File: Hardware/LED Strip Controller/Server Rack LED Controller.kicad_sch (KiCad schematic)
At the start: 76 parts

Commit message: Adding hardware schematic changes, added power regulation circuitry, stm32 filtering caps, labels
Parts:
- removed J?: Jack-DC, symbol Connector:Jack-DC
- added C10, C12, C13, C22, C27, C6, C8: 100nF, symbol Device:C
- added C11, C16: 100nF, Capacitor_SMD:C_1206_3216Metric_Pad1.33x1.80mm_HandSolder, symbol Device:C
- added C15, C9: 10nF, Capacitor_SMD:C_1206_3216Metric_Pad1.33x1.80mm_HandSolder, symbol Device:C
- added C17: 220u, Capacitor_SMD:CP_Elec_6.3x7.7, symbol Device:C_Polarized
- added C18, C20: 10uF, symbol Device:C_Polarized
- added C2, C23, C24, C3: C, symbol Device:C
- added C21, C25: 1uF, symbol Device:C
- added C4: 100uF, symbol Device:C_Polarized
- added C5: 1000u, Capacitor_SMD:CP_Elec_10x10.5, symbol Device:C_Polarized
- added C7: 680u, Capacitor_SMD:CP_Elec_6.3x7.7, symbol Device:C_Polarized
- added D13: 1N5821, Diode_SMD:D_SMA, symbol Diode:1N5821
- added D15, D22: LED, symbol Device:LED
- added D21: STPS2L30A, symbol pspice:DIODE
- added F1: Fuse, symbol Device:Fuse
- added FB?: FerriteBead, symbol Device:FerriteBead
- added J10, J5: Conn_01x03_Female, symbol Connector:Conn_01x03_Female
- added J15: Conn_01x06_Female, symbol Connector:Conn_01x06_Female
- added J4: Conn_02x03_Odd_Even, symbol Connector_Generic:Conn_02x03_Odd_Even
- added J8: Conn_01x04_Male, symbol Connector:Conn_01x04_Male
- added J9: USB_B_Micro, symbol Connector:USB_B_Micro
- added L1: 22u, Inductor_SMD:L_12x12mm_H8mm, symbol Device:L
- added Q3: Q_PMOS_SDG, Package_TO_SOT_SMD:TO-252-3_TabPin2, symbol Device:Q_PMOS_GDS
- added R14, R16, R22: R, symbol Device:R
- added R29, R30, R31, R32: 10K, symbol Device:R
- added R7: 10K, Resistor_SMD:R_1206_3216Metric_Pad1.30x1.75mm_HandSolder, symbol Device:R
- added SW1: SW_Push_Dual, symbol Switch:SW_Push_Dual
- added U2: LM2596S-5, Package_TO_SOT_SMD:TO-263-5_TabPin3, symbol Regulator_Switching:LM2596S-5
- added U3: LD1117S50TR_SOT223, Package_TO_SOT_SMD:SOT-223-3_TabPin2, symbol Regulator_Linear:LD1117S50TR_SOT223
- added U4: LD39050PU33R, SON95P300X300X100-7N, symbol LD39050PU33R:LD39050PU33R
- added Y1: Crystal, symbol Device:Crystal
- gave numbers to parts that had none: 75
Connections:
- net +5V: now also C21.1, C22.1, D21.2 (A), R22.1, U4.1 (EN), U4.6 (VIN); no longer J1.1 (Pin_1), J12.1 (Pin_1), J14.1 (Pin_1), J7.1 (Pin_1)
- net GND: now also C10.2, C11.2, C12.2, C13.2, C15.2, C16.2, C17.2, C18.2, C2.2, C20.2, C21.2, C22.2, C23.2, C24.2, C25.2, C27.2, C3.2, C4.2, C5.2, C6.2, C7.2, C8.2, C9.2, D13.2 (A), D15.1 (K), D22.1 (K), J10.3 (Pin_3), J15.6 (Pin_6), J4.1 (Pin_1), J4.2 (Pin_2), J5.3 (Pin_3), J8.4 (Pin_4), J9.5 (GND), J9.6 (Shield), R7.2, SW1.3, SW1.4, U2.3 (GND), U2.5 (~{ON}/OFF), U3.1 (GND), U4.2 (GND), U4.7 (GND)
- net PWM_1_BLUE: now also U1.17 (PA7)
- net PWM_1_GREEN: now also U1.19 (PB1)
- net PWM_1_RED: now also U1.18 (PB0)
- net PWM_2_BLUE: now also U1.11 (PA1)
- net PWM_2_GREEN: now also U1.13 (PA3)
- net PWM_2_RED: now also U1.12 (PA2)
- net PWM_3_BLUE: now also U1.45 (PB8)
- net PWM_3_GREEN: now also U1.42 (PB6)
- net PWM_3_RED: now also U1.43 (PB7)
- net PWM_4_BLUE: now also U1.46 (PB9)
- net PWM_4_GREEN: now also U1.10 (PA0)
- net PWM_4_RED: now also U1.16 (PA6)
- net STATUS_LED: now reaches U1.2 (PC13)
- net BOOT1: now reaches U1.20 (PB2)
- net BOOT1: now also J4.3 (Pin_3)
- net STM32_SCL2: now reaches U1.21 (PB10)
- net STM32_SCL2: now also J5.1 (Pin_1)
- net STM32_SDA2: now reaches U1.22 (PB11)
- net STM32_SDA2: now also J5.2 (Pin_2)
- net BUTTON_1: now reaches U1.26 (PB13)
- net BUTTON_1: now also J15.2 (Pin_2), R29.2
- net BUTTON_2: now reaches U1.27 (PB14)
- net BUTTON_2: now also J15.3 (Pin_3), R30.2
- net BUTTON_3: now reaches U1.28 (PB15)
- net BUTTON_3: now also J15.4 (Pin_4), R31.2
- net BUTTON_4: now reaches U1.29 (PA8)
- net BUTTON_4: now also J15.5 (Pin_5), R32.2
- net at U1.3 (PC14): now also C2.1, Y1.1
- net STM32_TX1: now reaches U1.30 (PA9)
- net STM32_TX1: now also J10.1 (Pin_1)
- net STM32_RX1: now reaches U1.31 (PA10)
- net STM32_RX1: now also J10.2 (Pin_2)
- net at U1.32 (PA11): now also J9.2 (D-)
- net at U1.33 (PA12): now also J9.3 (D+)
- net at U1.34 (PA13): now also J8.2 (Pin_2)
- net at U1.37 (PA14): now also J8.3 (Pin_3)
- net at U1.4 (PC15): now also C3.1, Y1.2
- net BOOT0: now reaches U1.44 (BOOT0)
- net BOOT0: now also J4.4 (Pin_4)
- net +VDC: no longer names the net of J3.1 (Pin_1)
- net +VDC: now also Q3.2 (D)
- new net: C20.1, D21.1 (K), U3.2 (VO)
- new net: D13.1 (K), L1.1, U2.2 (OUT)
- new net: F1.1, Q3.3 (S)
- new net: D22.2 (A), R22.2
- new net: FB?.1, U4.4 (VOUT)
- new net: Q3.1 (G), R7.1
- new net: D15.2 (A), R16.2
- new net: R14.2, SW1.1, SW1.2
- new net +3V3: C23.1, C24.1, C25.1, C27.1, FB?.2, J15.1 (Pin_1), R29.1, R30.1, R31.1, R32.1
- new net SMPS_5V: C15.1, C16.1, C17.1, J1.1 (Pin_1), J12.1 (Pin_1), J14.1 (Pin_1), J7.1 (Pin_1), L1.2, U2.4 (FB)
- new net VDD: C10.1, C12.1, C4.1, C6.1, C8.1, J4.5 (Pin_5), J4.6 (Pin_6), J8.1 (Pin_1), R14.1
- new net VDDA: C13.1
- new net Vss: C11.1, C18.1, C5.1, C7.1, C9.1, F1.2, U2.1 (VIN), U3.3 (VI)
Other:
- note added: "Input Power Circuitry"
- note added: "LED Strip Four"
- note added: "STM32 MCU Power"
- note removed: "Power Connectors"
- note removed: "SMPS"
- moved on the sheet: J14, J2, J3, J7, U1

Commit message: Adding updated PCB Schematic, still to add USB C connector and JLCPCB Part Numbers and values
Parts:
- removed J10: Conn_01x03_Female, symbol Connector:Conn_01x03_Female
- added C28, C31, C32: C, symbol Device:C
- added C29: 01.uF, Capacitor_SMD:C_1206_3216Metric, symbol Device:C
- added C30: 1uF, Capacitor_SMD:C_1206_3216Metric, symbol Device:C
- added D29: LED, symbol Device:LED
- added D30, D31: DIODE, symbol pspice:DIODE
- added J10: UART, Connector_PinHeader_2.54mm:PinHeader_1x03_P2.54mm_Vertical, symbol Connector:Conn_01x03_Male
- added J17: TST, symbol Connector:Conn_01x05_Male
- added J18, J19: Conn_01x03_Male, Connector_PinHeader_2.54mm:PinHeader_1x03_P2.54mm_Vertical, symbol Connector:Conn_01x03_Male
- added P1: USB_C_Plug, Connector_USB:USB_C_Receptacle_GCT_USB4085, symbol Connector:USB_C_Plug
- added Q14: IRF540N, Package_TO_SOT_THT:TO-220-3_Vertical, symbol Transistor_FET:IRF540N
- added R33, R34, R35, R36, R40, R41: R, symbol Device:R
- added R37, R39: 100K, Resistor_SMD:R_1206_3216Metric, symbol Device:R
- added R38: R, Resistor_SMD:R_1206_3216Metric, symbol Device:R
- added R42, R43, R46, R47: 20R, Resistor_SMD:R_1206_3216Metric, symbol Device:R
- added R44: 4.7K, Resistor_SMD:R_1206_3216Metric, symbol Device:R
- added R45: 1M, Resistor_SMD:R_1206_3216Metric, symbol Device:R
- added R48: 4.7K, symbol Device:R
- added U5: INA169, Package_TO_SOT_SMD:SOT-23-5, symbol Amplifier_Current:INA169
- added Y2: 8MHz, symbol Device:Crystal
- C1, C26: footprint (none) -> Capacitor_SMD:CP_Elec_10x10.5
- C10, C12, C13, C21, C22, C25, C27, C6, C8: footprint (none) -> Capacitor_SMD:C_1206_3216Metric
- C23: value C -> 100nF; footprint (none) -> Capacitor_SMD:C_1206_3216Metric
- C24: value C -> 10nF; footprint (none) -> Capacitor_SMD:C_1206_3216Metric
- D15, D22: footprint (none) -> LED_SMD:LED_1206_3216Metric
- J1, J12, J14, J7: footprint (none) -> Connector_PinHeader_2.54mm:PinHeader_1x03_P2.54mm_Vertical
- J11, J13, J16, J6: footprint (none) -> Connector_JST:JST_EH_B4B-EH-A_1x04_P2.50mm_Vertical
- J4: footprint (none) -> Connector_PinHeader_2.54mm:PinHeader_2x03_P2.54mm_Vertical
- J5: footprint (none) -> Connector_PinHeader_2.54mm:PinHeader_1x03_P2.54mm_Vertical; symbol Connector:Conn_01x03_Female -> Connector:Conn_01x03_Male
- J8: value Conn_01x04_Male -> SWD; footprint (none) -> Connector_PinHeader_2.54mm:PinHeader_1x04_P2.54mm_Vertical
- J9: footprint (none) -> Connector_USB:USB_Micro-B_Molex-105017-0001
- R1, R16, R2, R22, R23, R24, R25, R26, R27, R28, R29, R3, R30, R31, R32, R4, R5, R6: footprint (none) -> Resistor_SMD:R_1206_3216Metric
- R14: value R -> 10K; footprint (none) -> Resistor_SMD:R_1206_3216Metric
- SW1: footprint (none) -> Button_Switch_THT:SW_PUSH_6mm
- gave numbers to parts that had none: 1
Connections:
- net VDD is gone; now on net +3V3: C10.1, C12.1, C4.1, C6.1, C8.1, J4.5 (Pin_5), J4.6 (Pin_6), J8.1 (Pin_1), R14.1
- net VDDA is gone; now on net +3V3: C13.1
- net +3V3: now also R16.1, U1.24 (VDD), U1.36 (VDD), U1.48 (VDD), U1.9 (VDDA), C28.1, C29.1, J17.4 (Pin_4), U5.5 (V+)
- net +5V: now also J17.3 (Pin_3)
- net BOOT0: now also R39.2; no longer J4.4 (Pin_4)
- net BOOT1: now also R37.1; no longer J4.3 (Pin_3)
- net GND: now also U1.14 (PA4), U1.23 (VSS), U1.35 (VSS), U1.47 (VSS), U1.8 (VSSA), C28.2, C29.2, C30.2, C31.2, C32.2, D29.1 (K), J10.3 (Pin_3), J17.5 (Pin_5), P1.A1 (GND), P1.A12 (GND), P1.B1 (GND), P1.B12 (GND), Q14.3 (S), R34.1, R36.1, R41.2, U5.2 (GND)
- net PWM_1_BLUE: now also U1.12 (PA2); no longer U1.17 (PA7)
- net PWM_1_GREEN: now also U1.10 (PA0); no longer U1.19 (PB1)
- net PWM_1_RED: now also U1.11 (PA1); no longer U1.18 (PB0)
- net PWM_2_BLUE: now also U1.17 (PA7), U1.18 (PB0); no longer U1.11 (PA1)
- net PWM_2_GREEN: now also U1.16 (PA6); no longer U1.13 (PA3)
- net PWM_2_RED: no longer U1.12 (PA2)
- net PWM_4_GREEN: now also U1.13 (PA3); no longer U1.10 (PA0)
- net PWM_4_RED: now also U1.19 (PB1); no longer U1.16 (PA6)
- net SMPS_5V: now also D30.2 (A), J17.2 (Pin_2)
- net STATUS_LED: now also R38.1
- net STM32_RX1: now also J10.2 (Pin_2)
- net STM32_TX1: now also J10.1 (Pin_1)
- net Vss: now also J17.1 (Pin_1), R33.2, R35.2, U5.4 (-); no longer F1.2
- net OSC32_OUT: now reaches C3.1, U1.4 (PC15), Y1.2
- net OSC32_OUT: now also R45.2
- net USB_5V: now reaches J9.1 (VBUS)
- net USB_5V: now also R44.2, R48.2
- net at J9.2 (D-): now also R43.2; no longer U1.32 (PA11)
- net at J9.3 (D+): now also R42.2, R44.1; no longer U1.33 (PA12)
- net OSC32_IN: now reaches C2.1, U1.3 (PC14), Y1.1
- net OSC32_IN: now also R45.1
- net VS_SENSE: now reaches U1.15 (PA5)
- net VS_SENSE: now also R35.1, R36.2
- net FAN_SIG: now reaches U1.38 (PA15)
- net FAN_SIG: now also D31.2 (A), R40.2
- net OSC_IN: now reaches U1.5 (PD0)
- net OSC_IN: now also C31.1, Y2.1
- net OSC_OUT: now reaches U1.6 (PD1)
- net OSC_OUT: now also C32.1, Y2.2
- net RESET: now reaches U1.7 (NRST)
- net RESET: now also R14.2, SW1.1, SW1.2, C30.1
- new net: D29.2 (A), R38.2
- new net: D31.1 (K), Q14.1 (G), R40.1, R41.1
- new net: R34.2, U5.1
- new net: F1.2, R33.1, U5.3 (+)
- new net: R46.2, R48.1
- new net: D30.1 (K), Q14.2 (D)
- new net: J4.4 (Pin_4), R39.1
- new net: J4.3 (Pin_3), R37.2
- new net: P1.A4 (VBUS), P1.A9 (VBUS), P1.B4 (VBUS), P1.B9 (VBUS)
- new net STM32_USB+: J18.2 (Pin_2), U1.33 (PA12)
- new net STM32_USB-: J19.2 (Pin_2), U1.32 (PA11)
- new net STM32_USB_C+: J18.1 (Pin_1), J19.1 (Pin_1), R46.1
- new net STM32_USB_C-: R47.1
- new net STM32_USB_MICRO+: J18.3 (Pin_3), R42.1
- new net STM32_USB_MICRO-: J19.3 (Pin_3), R43.1
- no-connect marks 0 -> 4
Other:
- note added: "Boot"
- note added: "Button Daughterboard Connector"
- note added: "Fan Controller"
- note added: "RESET"
- note added: "USB C"
- note added: "USB Micro"
- note added: "USB Selector"
- moved on the sheet: C2, C3, D15, F1, J2, J3, J4, J8, J9, Q3, R14, R16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

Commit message: Adding updated PCB Schematic, need to source JLCPCB SMT Parts and do layout
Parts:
- removed J18, J19: Conn_01x03_Male, Connector_PinHeader_2.54mm:PinHeader_1x03_P2.54mm_Vertical, symbol Connector:Conn_01x03_Male
- removed P1: USB_C_Plug, Connector_USB:USB_C_Receptacle_GCT_USB4085, symbol Connector:USB_C_Plug
- removed R46, R47: 20R, Resistor_SMD:R_1206_3216Metric, symbol Device:R
- removed R48: 4.7K, symbol Device:R
- added C33: 1u, Capacitor_SMD:C_1206_3216Metric, symbol Device:C
- added C34: 10n, Capacitor_SMD:C_1206_3216Metric, symbol Device:C
- added J18: Conn_01x02_Female, Connector_JST:JST_EH_B2B-EH-A_1x02_P2.50mm_Vertical, symbol Connector:Conn_01x02_Female
- added L2: 39n, symbol pspice:INDUCTOR
- added U6: USBLC6-2SC6, Package_TO_SOT_SMD:SOT-23-6, symbol Power_Protection:USBLC6-2SC6
- C1, C26: value C_Polarized -> 100uF
- C14, C19: value C_Polarized -> 100uF; footprint (none) -> Capacitor_SMD:CP_Elec_10x10
- C18: footprint (none) -> Capacitor_SMD:CP_Elec_10x10.5
- C2, C3, C31, C32: footprint (none) -> Capacitor_SMD:C_1206_3216Metric
- C20, C4: footprint (none) -> Capacitor_SMD:CP_Elec_10x10
- C28: value C -> 01.uF; footprint (none) -> Capacitor_SMD:C_1206_3216Metric
- D1: value DIODE -> 1N4148; footprint (none) -> Diode_SMD:D_SOD-323; LCSC (none) -> C2128
- D10, D12, D17, D18, D20, D25, D26, D28, D9: value DIODE -> 1N4001; footprint (none) -> Diode_SMD:D_SMA
- D11, D14, D16, D19, D2, D23, D24, D27, D31, D5, D7, D8: value DIODE -> 1N4148; footprint (none) -> Diode_SMD:D_SOD-323
- D15: value LED -> Green LED
- D22: value LED -> Blue LED
- D29: value LED -> RED LED; footprint (none) -> LED_SMD:LED_1206_3216Metric
- D3, D4: value DIODE -> 1N4001; footprint (none) -> Diode_SMD:D_SOD-123F
- D30: value DIODE -> 1N5001; footprint (none) -> Diode_SMD:D_SMA
- D6: value DIODE -> 1N4001; footprint (none) -> Diode_SMD:D_SOD-123F; LCSC (none) -> C162732
- F1: value Fuse -> 1A; footprint (none) -> Fuse:Fuseholder_Clip-5x20mm_Eaton_1A5601-01_Inline_P20.80x6.76mm_D1.70mm_Horizontal
- J15: footprint (none) -> Connector_JST:JST_EH_B6B-EH-A_1x06_P2.50mm_Vertical
- J17: footprint (none) -> Connector_PinHeader_2.54mm:PinHeader_1x05_P2.54mm_Vertical
- J2, J3: footprint (none) -> TerminalBlock:TerminalBlock_bornier-2_P5.08mm
- Q1: value IRF540N -> IRF510N; footprint Package_TO_SOT_THT:TO-220-3_Vertical -> Package_TO_SOT_SMD:TO-263-3_TabPin2
- Q10, Q11, Q12, Q13, Q14, Q2, Q4, Q5, Q6, Q7, Q8, Q9: value IRF540N -> IRF510N; footprint Package_TO_SOT_THT:TO-220-3_Vertical -> Package_TO_SOT_SMD:TO-263-2
- R10, R11, R15, R18, R19, R34, R40, R8: value R -> 10K; footprint (none) -> Resistor_SMD:R_1206_3216Metric
- R12, R13, R17, R20, R21, R41, R9: value R -> 100K; footprint (none) -> Resistor_SMD:R_1206_3216Metric
- R16, R22, R38: value R -> 15K
- R23, R25, R26, R3, R4: value R -> 10K
- R24, R27, R28, R5, R6: value R -> 100K
- R33: value R -> 0.1R; footprint (none) -> Resistor_SMD:R_2512_6332Metric
- R35: value R -> 1M; footprint (none) -> Resistor_SMD:R_1206_3216Metric
- R36: value R -> 10M; footprint (none) -> Resistor_SMD:R_1206_3216Metric
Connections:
- net +3V3: now also L2.1; no longer C13.1, U1.9 (VDDA)
- net GND: now also C33.2, C34.2, U6.2 (GND); no longer J9.6 (Shield)
- net STM32_USB+: now also U6.1 (I/O1)
- net STM32_USB-: now also U6.6 (I/O1)
- net STM32_USB_MICRO+: now also U6.3 (I/O2)
- net STM32_USB_MICRO-: now also U6.4 (I/O2)
- net at D30.1 (K), Q14.2 (D): now also J18.2 (Pin_2)
- net SMPS_5V renamed PWR_5V
- net PWR_5V: now also J18.1 (Pin_1)
- net USB_5V renamed USB_VBUS
- net USB_VBUS: now also U6.5 (VBUS)
- new net VDDA: C13.1, C33.1, C34.1, L2.2, U1.9 (VDDA)
- no-connect marks 4 -> 8
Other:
- note added: "Analogue Power Filtering"
- note added: "D"
- note added: "G"
- note added: "MCU Power Filtering"
- note added: "MCU Power and GND"
- note added: "S"
- note added: "STM32 Power LED"
- note removed: "USB C"
- note removed: "USB Selector"
- moved on the sheet: C10, C11, C12, C13, C15, C16, C17, C28, C29, C4, C5, C6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

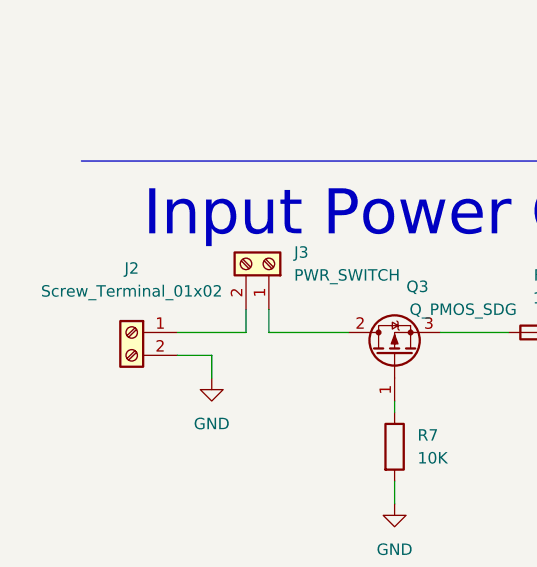
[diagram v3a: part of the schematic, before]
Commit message: Adding Kicad Schematic progress
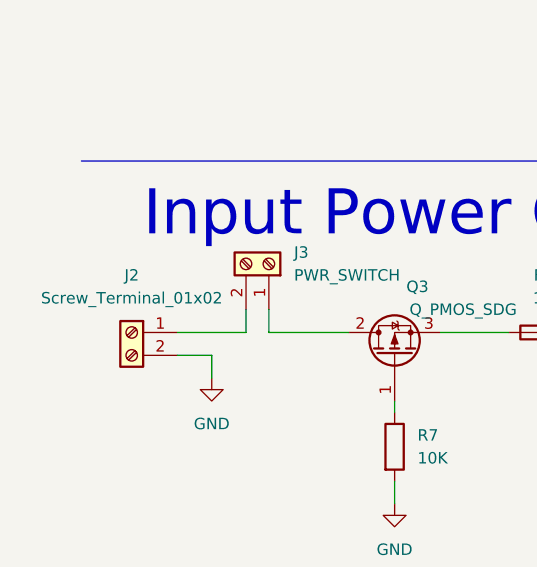
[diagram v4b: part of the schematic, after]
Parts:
- J2, J3: footprint TerminalBlock:TerminalBlock_bornier-2_P5.08mm -> TerminalBlock_Phoenix:TerminalBlock_Phoenix_MKDS-1,5-2-5.08_1x02_P5.08mm_Horizontal
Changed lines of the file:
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@@
   (symbol (lib_id "Connector:Screw_Terminal_01x02") (at 17.78 509.27 0) (mirror y) (unit 1)
     (in_bom yes) (on_board yes) (fields_autoplaced)
-    (property "Reference" "J2" (id 0) (at 17.78 502.158 0))
-    (property "Value" "Screw_Terminal_01x02" (id 1) (at 17.78 504.698 0))
-    (property "Footprint" "TerminalBlock:TerminalBlock_bornier-2_P5.08mm" (id 2) (at 17.78 509.27 0)
+    (property "Reference" "J2" (id 0) (at 17.78 502.92 0))
+    (property "Value" "Screw_Terminal_01x02" (id 1) (at 17.78 505.46 0))
+    (property "Footprint" "TerminalBlock_Phoenix:TerminalBlock_Phoenix_MKDS-1,5-2-5.08_1x02_P5.08mm_Horizontal" (id 2) (at 17.78 509.27 0)
       (effects (font (size 1.27 1.27)) hide)
     )
@@
       (effects (font (size 1.27 1.27)) (justify left))
     )
-    (property "Footprint" "TerminalBlock:TerminalBlock_bornier-2_P5.08mm" (id 2) (at 33.02 501.65 0)
+    (property "Footprint" "TerminalBlock_Phoenix:TerminalBlock_Phoenix_MKDS-1,5-2-5.08_1x02_P5.08mm_Horizontal" (id 2) (at 33.02 501.65 0)
       (effects (font (size 1.27 1.27)) hide)
     )
@@
     )
     (path "/b3c3b2d3-c28f-482e-9e67-413fada49294"
-      (reference "J2") (unit 1) (value "Screw_Terminal_01x02") (footprint "TerminalBlock:TerminalBlock_bornier-2_P5.08mm")
+      (reference "J2") (unit 1) (value "Screw_Terminal_01x02") (footprint "TerminalBlock_Phoenix:TerminalBlock_Phoenix_MKDS-1,5-2-5.08_1x02_P5.08mm_Horizontal")
     )
     (path "/b6d23dff-3660-46df-872f-37068fda7fff"
-      (reference "J3") (unit 1) (value "PWR_SWITCH") (footprint "TerminalBlock:TerminalBlock_bornier-2_P5.08mm")
+      (reference "J3") (unit 1) (value "PWR_SWITCH") (footprint "TerminalBlock_Phoenix:TerminalBlock_Phoenix_MKDS-1,5-2-5.08_1x02_P5.08mm_Horizontal")
     )
     (path "/7c1a5b26-d178-45d7-93d6-d3f5f5b864d0"

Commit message: Started layout of PCB
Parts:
- added C100, C39: 100uF, Capacitor_SMD:CP_Elec_6.3x7.7, symbol Device:C_Polarized
- added C35, C37: 10nF, Capacitor_SMD:C_1206_3216Metric_Pad1.33x1.80mm_HandSolder, symbol Device:C
- added C36, C38: 100nF, Capacitor_SMD:C_1206_3216Metric_Pad1.33x1.80mm_HandSolder, symbol Device:C
- added C40: 100uF, Capacitor_SMD:CP_Elec_10x10.5, symbol Device:C_Polarized
- added J19, J20: Conn_02x04_Odd_Even, Connector_PinHeader_2.54mm:PinHeader_2x04_P2.54mm_Vertical, symbol Connector_Generic:Conn_02x04_Odd_Even
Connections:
- net +3V3: now also C37.2, C38.1, C39.1, J20.2 (Pin_2), J20.4 (Pin_4), J20.6 (Pin_6), J20.8 (Pin_8)
- net +5V: now also C100.1, C35.2, C36.1, J19.2 (Pin_2), J19.4 (Pin_4), J19.6 (Pin_6), J19.8 (Pin_8)
- net GND: now also C100.2, C35.1, C36.2, C37.1, C38.2, C39.2, C40.2, J19.1 (Pin_1), J19.3 (Pin_3), J19.5 (Pin_5), J19.7 (Pin_7), J20.1 (Pin_1), J20.3 (Pin_3), J20.5 (Pin_5), J20.7 (Pin_7)
- net PWR_5V: now also C40.1
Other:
- note added: "Power Headers"

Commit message: Adding updated Layout, still need to finish it off, but parts are paired
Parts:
- J15: value Conn_01x06_Female -> Conn_01x06_Male; symbol Connector:Conn_01x06_Female -> Connector:Conn_01x06_Male
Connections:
- net D+: now reaches J9.3 (D+), R42.2, R44.1
- net D-: now reaches J9.2 (D-), R43.2
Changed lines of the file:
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@@
     (effects (font (size 1.27 1.27)) (justify left bottom))
   )
+  (label "D-" (at 312.42 284.48 0)
+    (effects (font (size 1.27 1.27)) (justify left bottom))
+  )
   (label "STM32_RX1" (at 125.73 312.42 0)
     (effects (font (size 1.27 1.27)) (justify left bottom))
@@
     (effects (font (size 1.27 1.27)) (justify left bottom))
   )
+  (label "D+" (at 312.42 281.94 0)
+    (effects (font (size 1.27 1.27)) (justify left bottom))
+  )
   (global_label "PWM_1_BLUE" (shape input) (at 48.7 136.6434 180) (fields_autoplaced)
     (effects (font (size 1.27 1.27)) (justify right))
@@
     (pin "2")
   )
-  (symbol (lib_id "Connector:Conn_01x06_Female") (at 410.21 289.56 0) (mirror y) (unit 1)
+  (symbol (lib_id "Connector:Conn_01x06_Male") (at 410.21 289.56 0) (unit 1)
     (in_bom yes) (on_board yes) (fields_autoplaced)
     (property "Reference" "J15" (id 0) (at 410.845 279.4 0))
-    (property "Value" "Conn_01x06_Female" (id 1) (at 410.845 281.94 0))
+    (property "Value" "Conn_01x06_Male" (id 1) (at 410.845 281.94 0))
     (property "Footprint" "Connector_JST:JST_EH_B6B-EH-A_1x06_P2.50mm_Vertical" (id 2) (at 410.21 289.56 0)
       (effects (font (size 1.27 1.27)) hide)
@@
     )
     (path "/79615b22-64eb-4a1f-8595-816ef3574fe6"
-      (reference "J15") (unit 1) (value "Conn_01x06_Female") (footprint "Connector_JST:JST_EH_B6B-EH-A_1x06_P2.50mm_Vertical")
+      (reference "J15") (unit 1) (value "Conn_01x06_Male") (footprint "Connector_JST:JST_EH_B6B-EH-A_1x06_P2.50mm_Vertical")
     )
     (path "/335b18b1-ecfb-4da7-9943-43ab56e337b4"
